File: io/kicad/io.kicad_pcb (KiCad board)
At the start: 2 copper layers, 90 x 88.4 mm, 51 parts, among them J1 Conn_01x04_Pin, J2 Conn_01x04_Pin, J3 pcie_98, U1 B0505MT-1WR4, U2 ESD5344D-TP, U3 ESD5344D-TP, U4 ADUM1201ARZ-RL7, U5 ADUM1201ARZ-RL7, U6 XC6206P332MR, U7 XC6206P332MR, U8 ESD5344D-TP

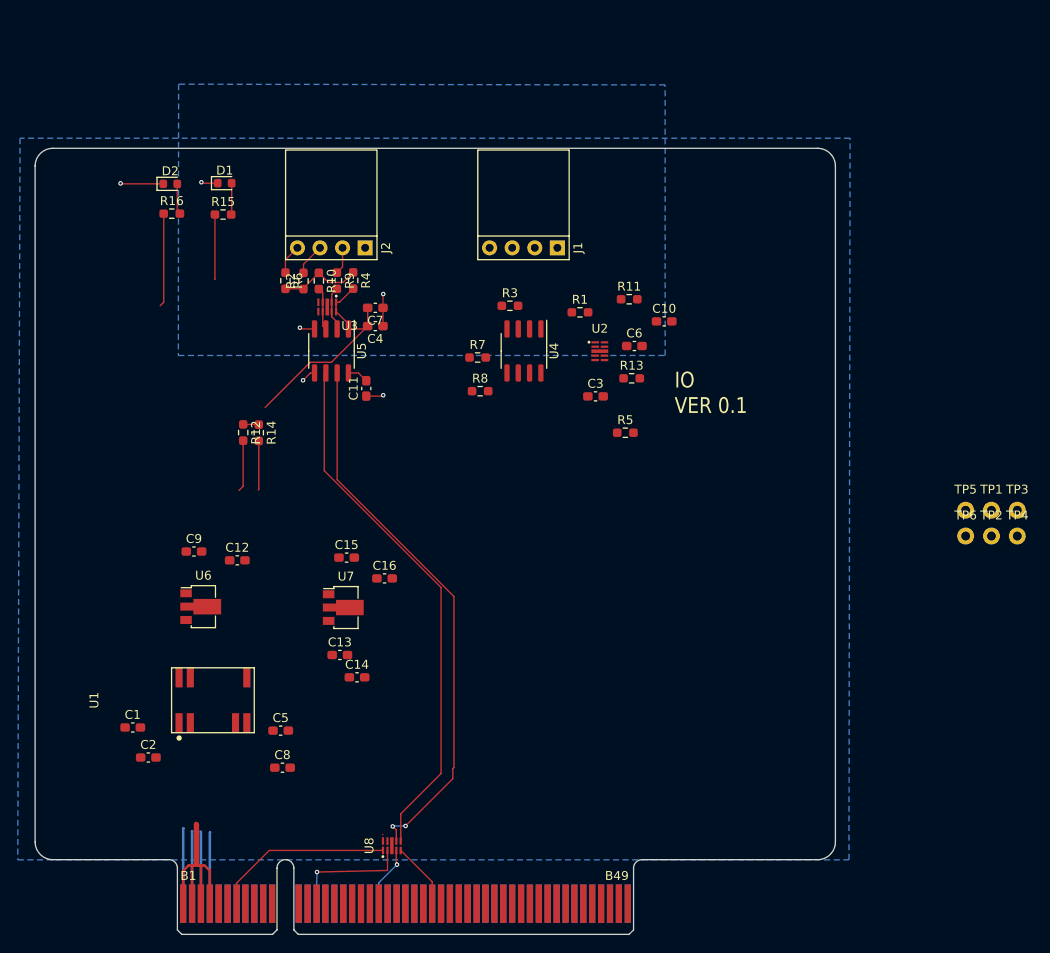
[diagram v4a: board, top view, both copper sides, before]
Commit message: Completed the topoligical routing of the IO board.
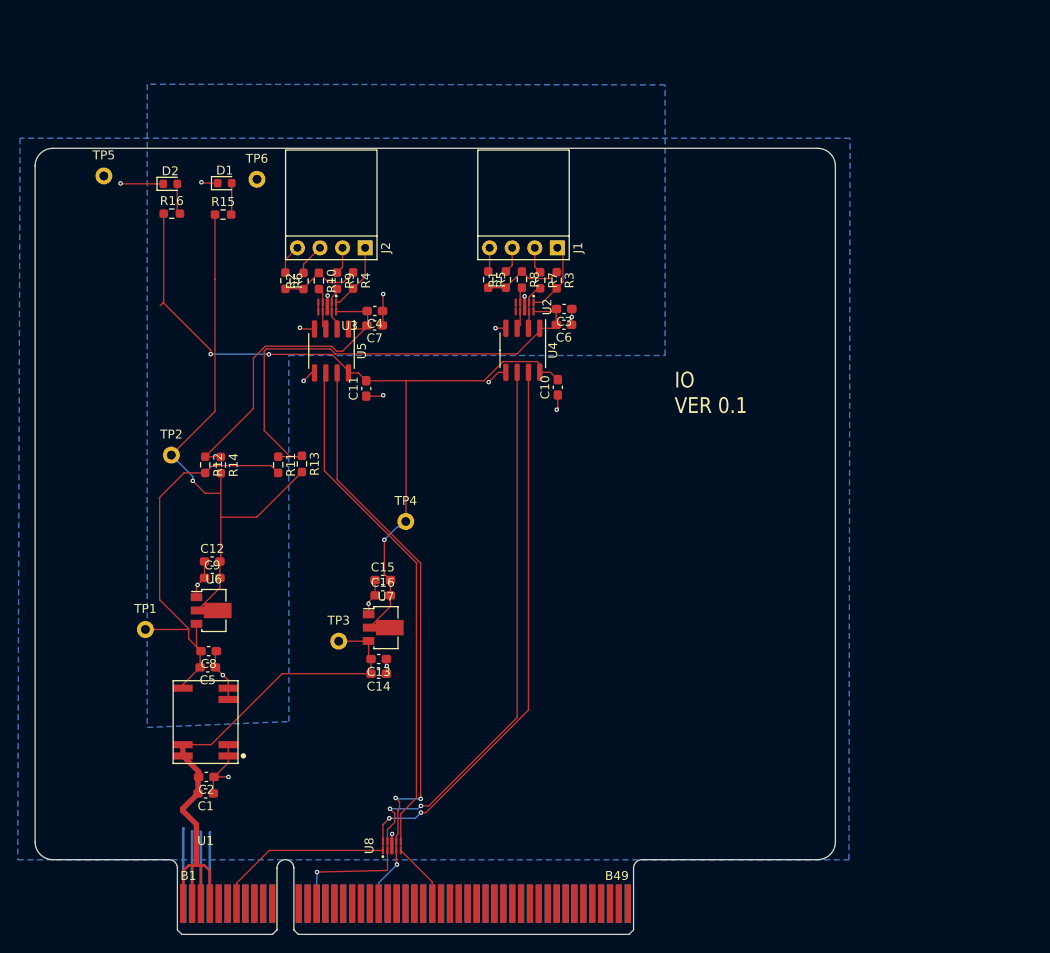
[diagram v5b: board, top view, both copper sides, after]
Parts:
- moved TP5 104.0 mm to (-20.4, -85.3)
- moved TP1 96.1 mm to (-15.7, -34.3)
- moved TP2 92.7 mm to (-12.8, -53.9)
- moved TP6 89.2 mm to (-3.20, -84.9)
- moved TP3 77.7 mm to (5.99, -33.0)
- moved TP4 68.8 mm to (13.5, -46.4)
- moved R11 43.6 mm to (-0.81, -52.8), turned to -90 degrees
- moved R13 38.3 mm to (1.85, -52.9), turned to -90 degrees
- moved R5 23.1 mm to (22.8, -73.6), turned to -90 degrees
- moved C8 15.5 mm to (-8.64, -31.9), turned to 180 degrees
- moved C10 14.1 mm to (30.6, -61.5), turned to 90 degrees
- moved R8 13.4 mm to (26.6, -73.6), turned to -90 degrees
- moved R7 11.2 mm to (28.7, -73.6), turned to -90 degrees
- moved C1 11.1 mm to (-8.97, -15.8), turned to 180 degrees
- moved C5 10.9 mm to (-8.74, -30.0), turned to 180 degrees
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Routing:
- net +3.3V: track 12.9 -> 91.9 mm, vias 0 -> 3
- net Net-(J1-Pin_1): track 0.00 -> 64.4 mm
- net /PC6: track 13.7 -> 76.4 mm, vias 1 -> 3
- net /PC7: track 20.3 -> 82.9 mm, vias 0 -> 2
- net /+3V3F: track 12.8 -> 64.4 mm, vias 0 -> 1
- net +5V: track 24.9 -> 67.6 mm
- net /+5VF: track 5.81 -> 47.6 mm
- net Net-(J2-Pin_1): track 27.8 -> 47.3 mm
- net GND: track 41.3 -> 60.4 mm, vias 3 -> 9
- net GND1: track 10.5 -> 29.2 mm, vias 3 -> 9
- net Net-(R1-Pad1): track 0.00 -> 9.09 mm
- net Net-(U2-D2): track 0.00 -> 5.19 mm
- net Net-(U2-D3): track 0.00 -> 4.78 mm
- net Net-(J1-Pin_2): track 0.00 -> 2.99 mm
- net Net-(J1-Pin_3): track 0.00 -> 2.95 mm
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
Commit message: IO layout passes DRC.
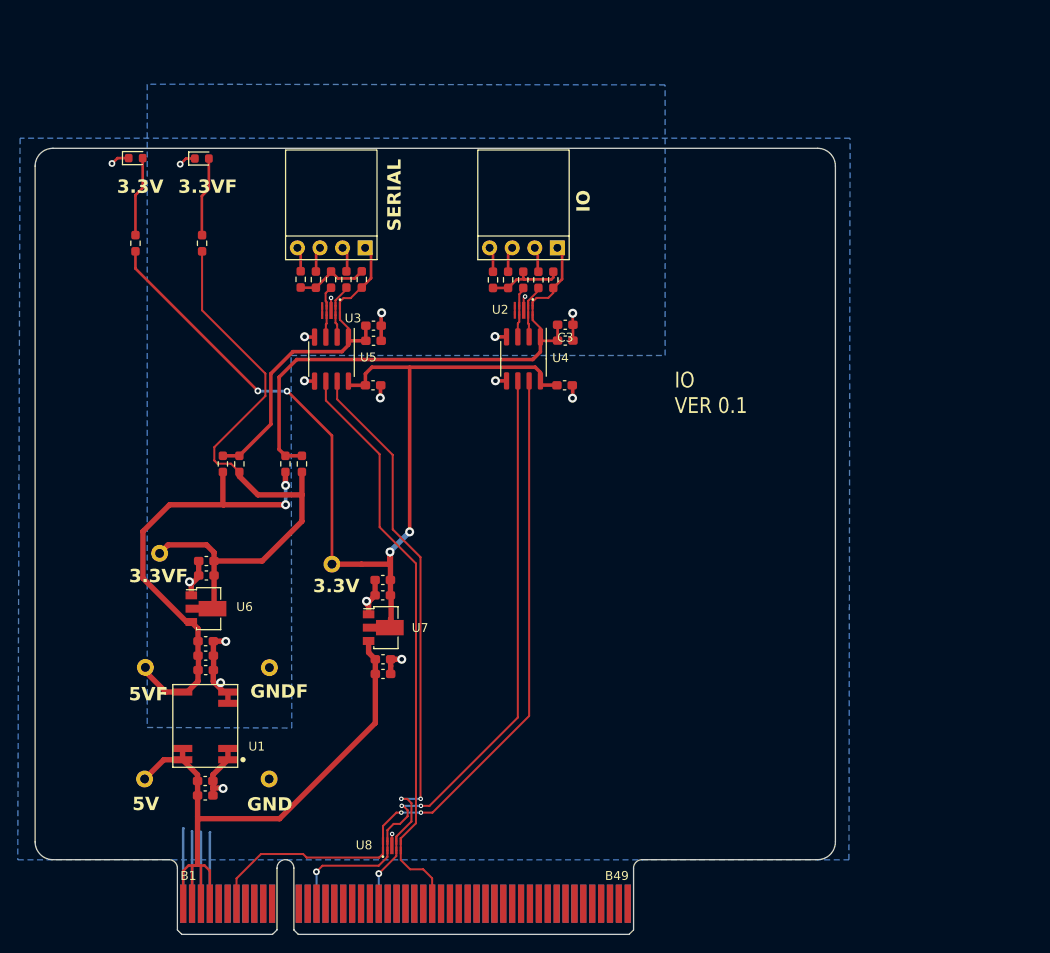
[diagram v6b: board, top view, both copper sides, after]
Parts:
- added C17: 100n, Capacitor_SMD:C_0603_1608Metric_Pad1.08x0.95mm_HandSolder, F.Cu at (-8.97, -33.0)
- moved TP5 70.3 mm to (-1.83, -17.5)
- moved TP6 54.9 mm to (-1.80, -30.0)
- moved TP3 26.8 mm to (-15.8, -17.5)
- moved TP2 11.1 mm to (-14.1, -42.8)
- moved TP4 9.59 mm to (5.23, -41.6)
- moved R16 5.27 mm to (-16.9, -77.7), turned to 90 degrees
- moved D2 4.85 mm to (-16.8, -87.3)
- moved TP1 4.27 mm to (-15.7, -30.0)
- moved R15 4.00 mm to (-9.37, -77.7), turned to 90 degrees
- moved D1 3.77 mm to (-9.40, -87.2)
- moved R14 2.09 mm to (-5.18, -52.9)
- moved R12 1.98 mm to (-7.04, -52.9)
- moved C6 1.78 mm to (31.5, -66.8)
- moved C3 1.78 mm to (31.5, -68.6)
- moved C7 1.73 mm to (9.91, -66.8)
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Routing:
- net +3.3V: track 91.9 -> 110.1 mm, vias 3 -> 4
- net Net-(J2-Pin_1): track 47.3 -> 39.3 mm
- net /+3V3F: track 64.4 -> 70.8 mm, vias 1 -> 0
- net +5V: track 67.6 -> 73.3 mm
- net Net-(D2-A): track 3.48 -> 9.00 mm
- net Net-(D1-A): track 3.55 -> 8.95 mm
- net Net-(J1-Pin_1): track 64.4 -> 59.1 mm
- net /+5VF: track 47.6 -> 52.4 mm, vias 0 -> 2
- net GND1: track 29.2 -> 33.4 mm, vias 9 -> 10
- net GND: track 60.4 -> 58.2 mm
- net /PC6: track 76.4 -> 74.8 mm
- net Net-(R10-Pad1): track 9.36 -> 8.36 mm
- net Net-(U2-D3): track 4.78 -> 5.76 mm
- net Net-(U3-D2): track 5.05 -> 6.00 mm
- net Net-(U2-D2): track 5.19 -> 6.02 mm
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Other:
- board text added: "3.3V"
- board text added: "3.3VF"
- board text added: "5V"
- board text added: "5VF"
- board text added: "GND"
- board text added: "GNDF"
- board text added: "IO"
- board text added: "SERIAL"

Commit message: Tweaked IO board layout.
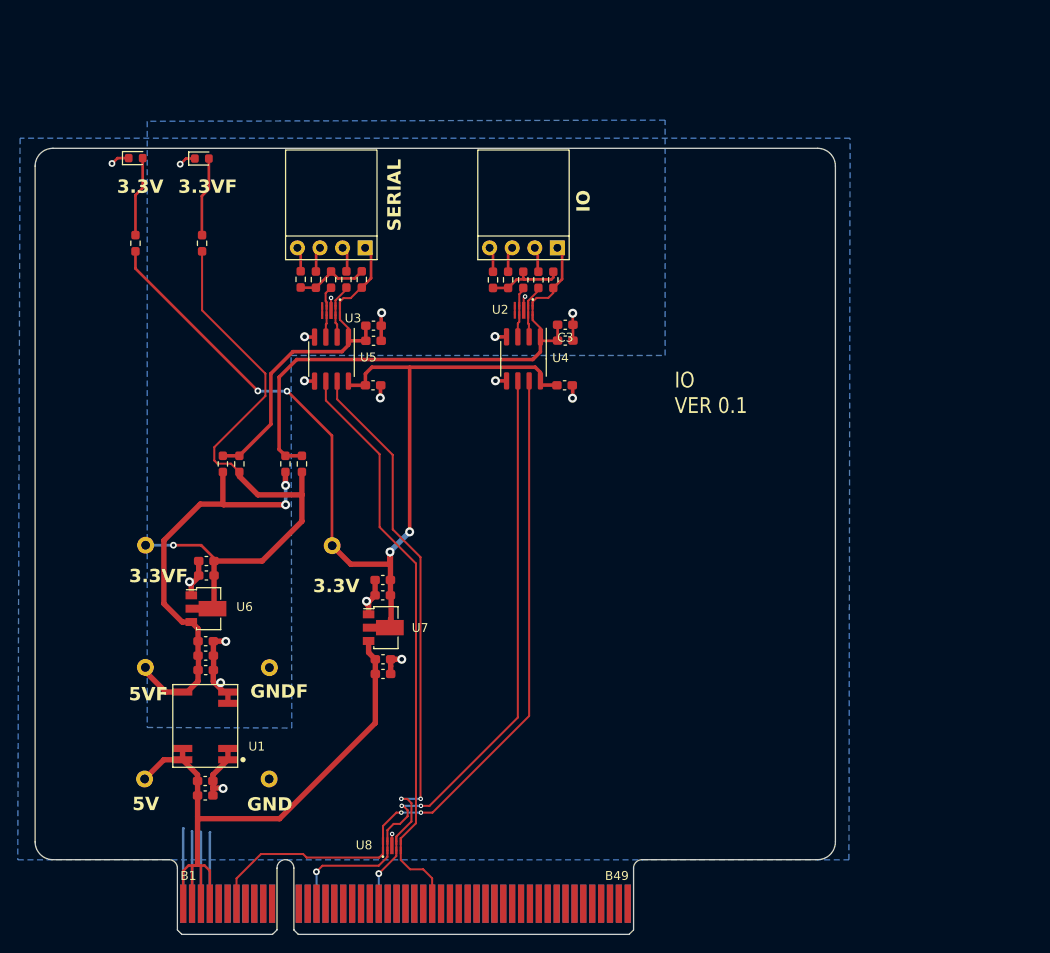
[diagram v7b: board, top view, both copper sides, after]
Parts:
- moved TP4 2.08 mm to (5.26, -43.7)
- moved TP2 1.82 mm to (-15.7, -43.8)
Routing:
- net /+5VF: track 52.4 -> 48.7 mm
- net +3.3V: track 110.1 -> 108.8 mm
- net /+3V3F: track 70.8 -> 71.6 mm, vias 0 -> 1
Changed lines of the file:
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@@
   )
   (footprint "common:Test_Pad" (layer "F.Cu")
-    (at -14.1478 -42.8498)
+    (at -15.7226 -43.7642)
     (descr "Through hole straight pin header, 1x02, 2.54mm pitch, single row")
     (tags "Through hole pin header THT 1x02 2.54mm single row")
@@
   )
   (footprint "common:Test_Pad" (layer "F.Cu")
-    (at 5.2324 -41.6306)
+    (at 5.2578 -43.7134)
     (descr "Through hole straight pin header, 1x02, 2.54mm pitch, single row")
     (tags "Through hole pin header THT 1x02 2.54mm single row")
@@
   (via (at -11.8364 -86.614) (size 0.762) (drill 0.381) (layers "F.Cu" "B.Cu") (net 2))
   (via (at 26.9494 -71.7296) (size 0.508) (drill 0.254) (layers "F.Cu" "B.Cu") (net 2))
-  (segment (start -16.0274 -45.3136) (end -13.0302 -48.3108) (width 0.6096) (layer "F.Cu") (net 3))
   (segment (start -7.0358 -48.387) (end -6.9596 -48.3108) (width 0.6096) (layer "F.Cu") (net 3))
-  (segment (start -11.1004 -35.1268) (end -16.0274 -40.0538) (width 0.6096) (layer "F.Cu") (net 3))
+  (segment (start -11.6064 -35.1268) (end -13.6652 -37.1856) (width 0.6096) (layer "F.Cu") (net 3))
   (segment (start -7.0358 -51.9957) (end -7.0358 -48.387) (width 0.6096) (layer "F.Cu") (net 3))
   (segment (start -9.8287 -28.4745) (end -9.8287 -29.718) (width 0.6096) (layer "F.Cu") (net 3))
+  (segment (start -10.586 -35.1268) (end -11.6064 -35.1268) (width 0.6096) (layer "F.Cu") (net 3))
   (segment (start 0.0254 -50.5714) (end 0.0254 -50.4952) (width 0.6096) (layer "F.Cu") (net 3))
   (segment (start -9.8287 -31.3436) (end -9.8287 -32.9692) (width 0.6096) (layer "F.Cu") (net 3))
@@
   (segment (start -9.7779 -31.3436) (end -9.7779 -29.7434) (width 0.6096) (layer "F.Cu") (net 3))
   (segment (start -9.8287 -32.9692) (end -9.8287 -34.3695) (width 0.6096) (layer "F.Cu") (net 3))
-  (segment (start -13.0302 -48.3108) (end -6.9596 -48.3108) (width 0.6096) (layer "F.Cu") (net 3))
-  (segment (start -10.586 -35.1268) (end -11.1004 -35.1268) (width 0.6096) (layer "F.Cu") (net 3))
   (segment (start -13.4484 -27.2542) (end -15.748 -29.5538) (width 0.6096) (layer "F.Cu") (net 3))
   (segment (start -11.049 -27.2542) (end -9.8287 -28.4745) (width 0.6096) (layer "F.Cu") (net 3))
   (segment (start -6.9596 -48.3108) (end 0.0254 -48.3108) (width 0.6096) (layer "F.Cu") (net 3))
   (segment (start -11.567 -27.2542) (end -11.049 -27.2542) (width 0.6096) (layer "F.Cu") (net 3))
-  (segment (start -16.0274 -40.0538) (end -16.0274 -45.3136) (width 0.6096) (layer "F.Cu") (net 3))
   (segment (start -15.748 -29.5538) (end -15.748 -30.0228) (width 0.6096) (layer "F.Cu") (net 3))
+  (segment (start -13.6652 -37.1856) (end -13.6652 -44.2976) (width 0.6096) (layer "F.Cu") (net 3))
   (segment (start -9.8287 -34.3695) (end -10.586 -35.1268) (width 0.6096) (layer "F.Cu") (net 3))
   (segment (start -11.567 -27.2542) (end -13.4484 -27.2542) (width 0.6096) (layer "F.Cu") (net 3))
+  (segment (start -13.6652 -44.2976) (end -9.5758 -48.387) (width 0.6096) (layer "F.Cu") (net 3))
   (segment (start 0.1016 -50.4952) (end 0.0254 -50.5714) (width 0.6096) (layer "F.Cu") (net 3))
   (segment (start 0.0254 -50.4952) (end 0.1016 -50.4952) (width 0.6096) (layer "F.Cu") (net 3))
+  (segment (start -9.5758 -48.387) (end -7.0358 -48.387) (width 0.6096) (layer "F.Cu") (net 3))
   (via (at 0.0254 -50.4952) (size 1.016) (drill 0.508) (layers "F.Cu" "B.Cu") (net 3))
   (via (at 0.0254 -48.3108) (size 1.016) (drill 0.508) (layers "F.Cu" "B.Cu") (net 3))
@@
   (segment (start -8.001 -54.7878) (end -2.25301 -60.53579) (width 0.2286) (layer "F.Cu") (net 4))
   (segment (start 1.8542 -49.403) (end 1.8288 -49.4284) (width 0.6096) (layer "F.Cu") (net 4))
+  (segment (start -9.4742 -43.7642) (end -12.5984 -43.7642) (width 0.3048) (layer "F.Cu") (net 4))
   (segment (start -5.1816 -51.9957) (end -6.1195 -52.9336) (width 0.2286) (layer "F.Cu") (net 4))
   (segment (start -5.1816 -51.5112) (end -5.1816 -51.9957) (width 0.6096) (layer "F.Cu") (net 4))
   (segment (start 1.8288 -49.4284) (end -3.0988 -49.4284) (width 0.6096) (layer "F.Cu") (net 4))
-  (segment (start -14.1478 -42.8498) (end -13.1953 -43.8023) (width 0.6096) (layer "F.Cu") (net 4))
   (segment (start -8.001 -53.2892) (end -8.001 -54.7878) (width 0.2286) (layer "F.Cu") (net 4))
+  (segment (start -8.0286 -42.3186) (end -9.4742 -43.7642) (width 0.3048) (layer "F.Cu") (net 4))
   (segment (start 1.8542 -46.4566) (end 1.8542 -49.403) (width 0.6096) (layer "F.Cu") (net 4))
-  (segment (start -8.0286 -42.9536) (end -8.0286 -41.9862) (width 0.6096) (layer "F.Cu") (net 4))
   (segment (start -2.25301 -63.06061) (end -9.3726 -70.1802) (width 0.2286) (layer "F.Cu") (net 4))
   (segment (start -8.0286 -41.9862) (end -2.6162 -41.9862) (width 0.6096) (layer "F.Cu") (net 4))
   (segment (start -8.0275 -40.2082) (end -8.0264 -40.2071) (width 0.6096) (layer "F.Cu") (net 4))
   (segment (start -9.3726 -70.1802) (end -9.3726 -76.8115) (width 0.2286) (layer "F.Cu") (net 4))
-  (segment (start -8.8773 -43.8023) (end -8.0286 -42.9536) (width 0.6096) (layer "F.Cu") (net 4))
   (segment (start -7.6454 -52.9336) (end -8.001 -53.2892) (width 0.2286) (layer "F.Cu") (net 4))
   (segment (start -6.1195 -52.9336) (end -7.6454 -52.9336) (width 0.2286) (layer "F.Cu") (net 4))
   (segment (start -8.0264 -40.2071) (end -8.0264 -36.72895) (width 0.6096) (layer "F.Cu") (net 4))
-  (segment (start -13.1953 -43.8023) (end -8.8773 -43.8023) (width 0.6096) (layer "F.Cu") (net 4))
   (segment (start -8.0286 -41.8846) (end -8.0286 -40.2093) (width 0.6096) (layer "F.Cu") (net 4))
+  (segment (start -8.0286 -41.9862) (end -8.0286 -42.3186) (width 0.3048) (layer "F.Cu") (net 4))
   (segment (start -2.25301 -60.53579) (end -2.25301 -63.06061) (width 0.2286) (layer "F.Cu") (net 4))
   (segment (start -3.0988 -49.4284) (end -5.1816 -51.5112) (width 0.6096) (layer "F.Cu") (net 4))
@@
   (segment (start -8.0286 -40.2093) (end -8.0275 -40.2082) (width 0.6096) (layer "F.Cu") (net 4))
   (segment (start -2.6162 -41.9862) (end 1.8542 -46.4566) (width 0.6096) (layer "F.Cu") (net 4))
+  (via (at -12.5984 -43.7642) (size 0.762) (drill 0.381) (layers "F.Cu" "B.Cu") (net 4))
+  (segment (start -15.6972 -43.7642) (end -12.5984 -43.7642) (width 0.3048) (layer "B.Cu") (net 4))
   (segment (start -10.8966 -7.747) (end -11.5 -7.1436) (width 0.2794) (layer "F.Cu") (net 5))
   (segment (start -9.9822 -7.747) (end -10.8966 -7.747) (width 0.2794) (layer "F.Cu") (net 5))
@@
   (segment (start 28.6766 -63.1952) (end 28.6766 -62.2442) (width 0.4064) (layer "F.Cu") (net 6))
   (segment (start -16.8656 -74.8792) (end -3.0988 -61.1124) (width 0.3048) (layer "F.Cu") (net 6))
+  (segment (start 0.2286 -61.087) (end 0.1778 -61.087) (width 0.3048) (layer "F.Cu") (net 6))
+  (segment (start 7.3406 -41.6306) (end 11.7602 -41.6306) (width 0.6096) (layer "F.Cu") (net 6))
   (segment (start 30.27735 -61.7728) (end 28.75225 -61.7728) (width 0.4064) (layer "F.Cu") (net 6))
   (segment (start 11.8872 -34.46835) (end 11.8872 -38.0481) (width 0.6096) (layer "F.Cu") (net 6))
-  (segment (start 5.2324 -41.6306) (end 5.2324 -56.0832) (width 0.3048) (layer "F.Cu") (net 6))
-  (segment (start 5.2324 -56.0832) (end 0.2286 -61.087) (width 0.3048) (layer "F.Cu") (net 6))
   (segment (start 11.8099 -42.9525) (end 11.8099 -39.8526) (width 0.6096) (layer "F.Cu") (net 6))
   (segment (start 13.97 -63.7794) (end 13.97 -45.262798) (width 0.4064) (layer "F.Cu") (net 6))
   (segment (start 8.77625 -61.7474) (end 7.17495 -61.7474) (width 0.4064) (layer "F.Cu") (net 6))
   (segment (start 11.8872 -38.0481) (end 11.8099 -38.1254) (width 0.6096) (layer "F.Cu") (net 6))
-  (segment (start 8.5598 -41.6306) (end 11.7602 -41.6306) (width 0.6096) (layer "F.Cu") (net 6))
+  (segment (start 5.2324 -56.0832) (end 0.2286 -61.087) (width 0.3048) (layer "F.Cu") (net 6))
   (segment (start 11.8099 -38.1254) (end 11.8099 -39.8526) (width 0.6096) (layer "F.Cu") (net 6))
   (segment (start 11.7602 -43.0022) (end 11.8099 -42.9525) (width 0.6096) (layer "F.Cu") (net 6))
+  (segment (start 5.2324 -43.7388) (end 5.2324 -56.0832) (width 0.3048) (layer "F.Cu") (net 6))
   (segment (start 8.9927 -61.7474) (end 8.9927 -63.0439) (width 0.4064) (layer "F.Cu") (net 6))
+  (segment (start 5.2578 -43.7134) (end 7.3406 -41.6306) (width 0.6096) (layer "F.Cu") (net 6))
   (segment (start 11.8099 -35.4341) (end 11.811 -35.433) (width 0.6096) (layer "F.Cu") (net 6))
-  (segment (start 5.2324 -41.6306) (end 8.5598 -41.6306) (width 0.6096) (layer "F.Cu") (net 6))
+  (segment (start 5.2578 -43.7134) (end 5.2324 -43.7388) (width 0.3048) (layer "F.Cu") (net 6))
   (segment (start 8.9927 -63.0439) (end 9.7282 -63.7794) (width 0.4064) (layer "F.Cu") (net 6))
   (segment (start 9.7282 -63.7794) (end 28.0924 -63.7794) (width 0.4064) (layer "F.Cu") (net 6))
   (segment (start 28.0924 -63.7794) (end 28.6766 -63.1952) (width 0.4064) (layer "F.Cu") (net 6))
   (segment (start 11.7602 -41.6306) (end 11.7602 -43.0022) (width 0.6096) (layer "F.Cu") (net 6))
-  (segment (start 0.2286 -61.087) (end 0.1778 -61.087) (width 0.3048) (layer "F.Cu") (net 6))
   (via (at 11.7602 -43.0022) (size 1.016) (drill 0.508) (layers "F.Cu" "B.Cu") (net 6))
   (via (at -3.0988 -61.1124) (size 0.762) (drill 0.381) (layers "F.Cu" "B.Cu") (net 6))
@@
     (polygon
       (pts
-        (xy -15.5448 -95.6056)
+        (xy -15.5448 -91.44)
         (xy -15.5448 -23.2664)
         (xy 0.7112 -23.203344)
         (xy 0.635 -65.1002)
         (xy 42.6974 -65.1002)
-        (xy 42.6974 -95.5294)
+        (xy 42.6974 -91.567)
       )
     )
